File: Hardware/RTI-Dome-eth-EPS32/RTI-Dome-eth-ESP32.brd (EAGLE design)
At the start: 111.1 x 76.3 mm, 100 parts, among them IC1 REG1117FA-5.0_500, IC2 24LC64T-I/SN, IC8 REG1117-3.3V, J2 XT60PW-M, T1 MMBT3904LT1, T2 MMBT3904LT1, T3 MMBT3904LT1, U1 W5500, U2 ESP32-DevKitC ESP32-WROOM-32U, X9 J1011F01PNL

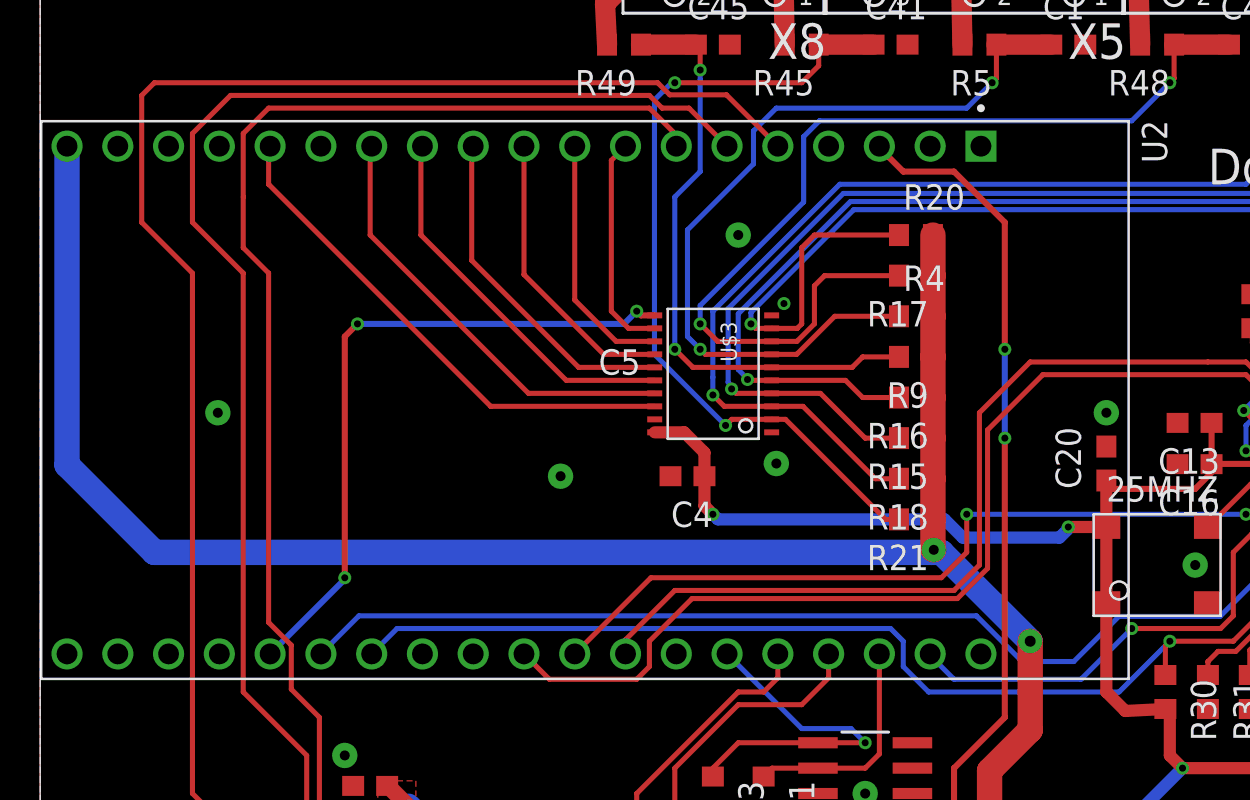
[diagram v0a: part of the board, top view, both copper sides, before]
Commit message: Set the proper version of the EXP32 kit for each board.
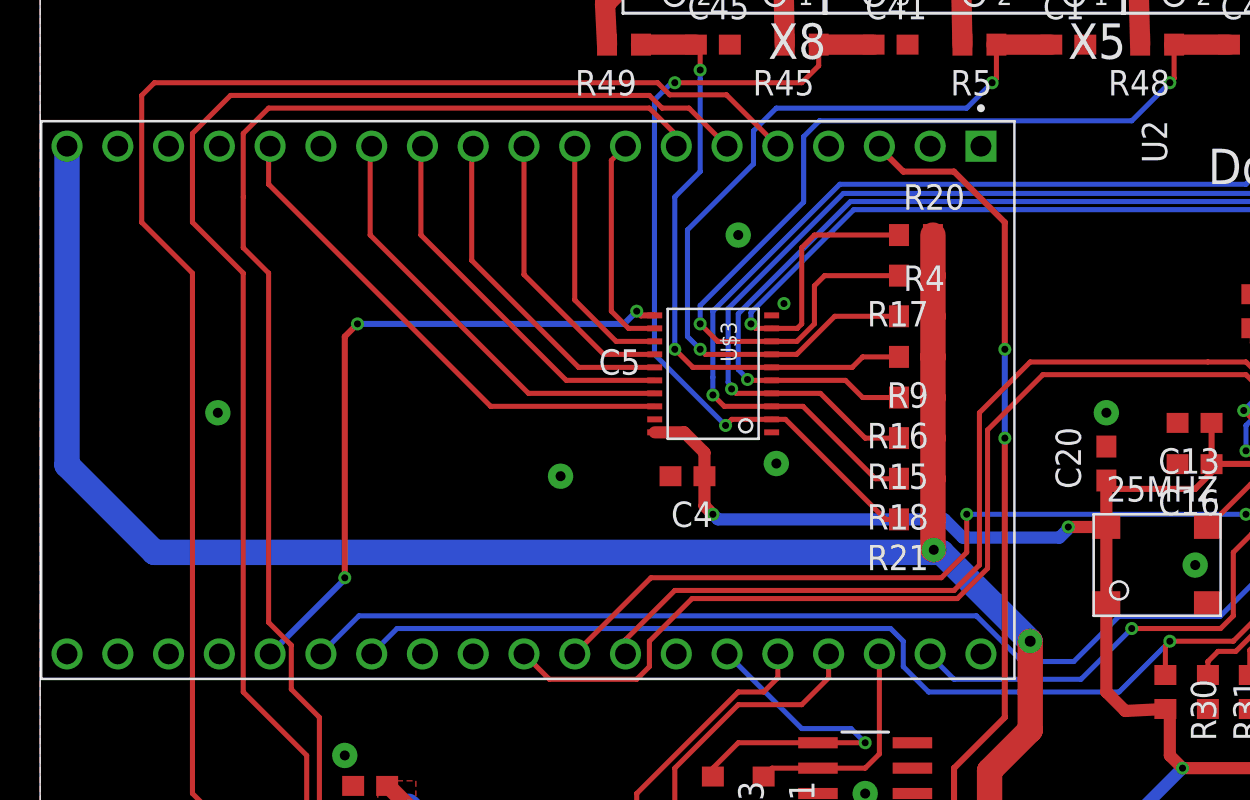
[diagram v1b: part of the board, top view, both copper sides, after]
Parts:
- U2: device ESP32-DEVKITC-32D:MODULE_ESP32-DEVKITC-32D -> ESP32-DEVKITC-32D:MODULE_ESP32-DEVKITC-32U
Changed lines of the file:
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@@
 <attribute name="VALUE" x="81.28" y="17" size="1.27" layer="27" align="center"/>
 </element>
-<element name="U2" library="ESP32-DEVKITC-32D" library_urn="urn:adsk.eagle:library:44270575" package="MODULE_ESP32-DEVKITC-32D" package3d_urn="urn:adsk.eagle:package:44270578/3" value="ESP32-DevKitC ESP32-WROOM-32U" x="27.305" y="46.99" smashed="yes" rot="R270">
-<attribute name="AVAILABILITY" value="In Stock" x="27.305" y="46.99" size="1.778" layer="27" rot="R270" display="off"/>
-<attribute name="CHECK_PRICES" value="https://www.snapeda.com/parts/ESP32-DEVKITC-32D/Espressif+Systems/view-part/?ref=eda" x="27.305" y="46.99" size="1.778" layer="27" rot="R270" display="off"/>
-<attribute name="DESCRIPTION" value=" WiFi Development Tools (802.11) ESP32 General Development Kit, ESP32-WROOM-32D on the board " x="27.305" y="46.99" size="1.778" layer="27" rot="R270" display="off"/>
-<attribute name="MF" value="Espressif Systems" x="27.305" y="46.99" size="1.778" layer="27" rot="R270" display="off"/>
-<attribute name="MP" value="ESP32-DEVKITC-32D" x="27.305" y="46.99" size="1.778" layer="27" rot="R270" display="off"/>
+<element name="U2" library="ESP32-DEVKITC-32D" library_urn="urn:adsk.eagle:library:44270575" package="MODULE_ESP32-DEVKITC-32U" package3d_urn="urn:adsk.eagle:package:44294361/2" value="ESP32-DevKitC ESP32-WROOM-32U" x="27.305" y="46.99" smashed="yes" rot="R270">
 <attribute name="NAME" x="55.1158" y="60.9954" size="1.270490625" layer="25" rot="R270"/>
-<attribute name="PACKAGE" value="None" x="27.305" y="46.99" size="1.778" layer="27" rot="R270" display="off"/>
-<attribute name="PRICE" value="None" x="27.305" y="46.99" size="1.778" layer="27" rot="R270" display="off"/>
-<attribute name="SNAPEDA_LINK" value="https://www.snapeda.com/parts/ESP32-DEVKITC-32D/Espressif+Systems/view-part/?ref=snap" x="27.305" y="46.99" size="1.778" layer="27" rot="R270" display="off"/>
 <attribute name="VALUE" x="-1.6252" y="61.0046" size="1.27133125" layer="27" rot="R270"/>
 </element>

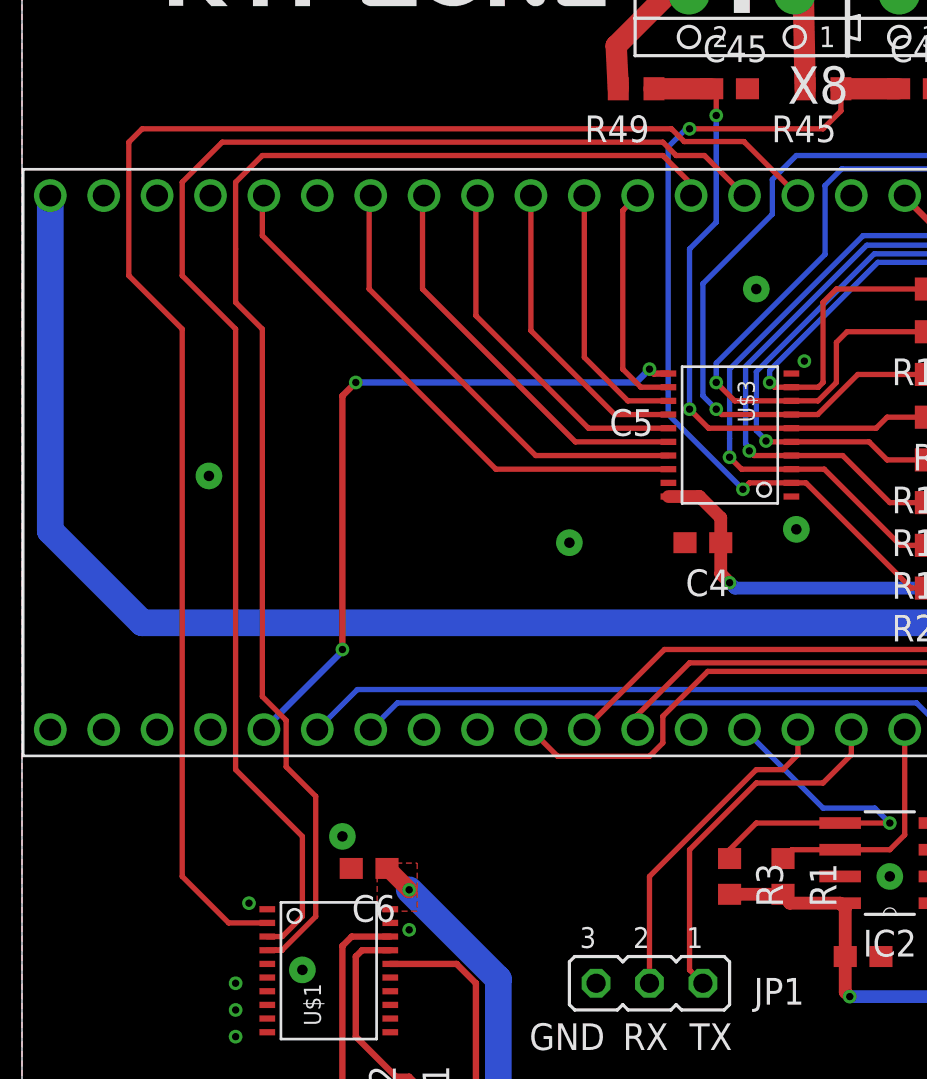
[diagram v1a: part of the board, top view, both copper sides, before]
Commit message: Fix pin assignement issues for ESP32
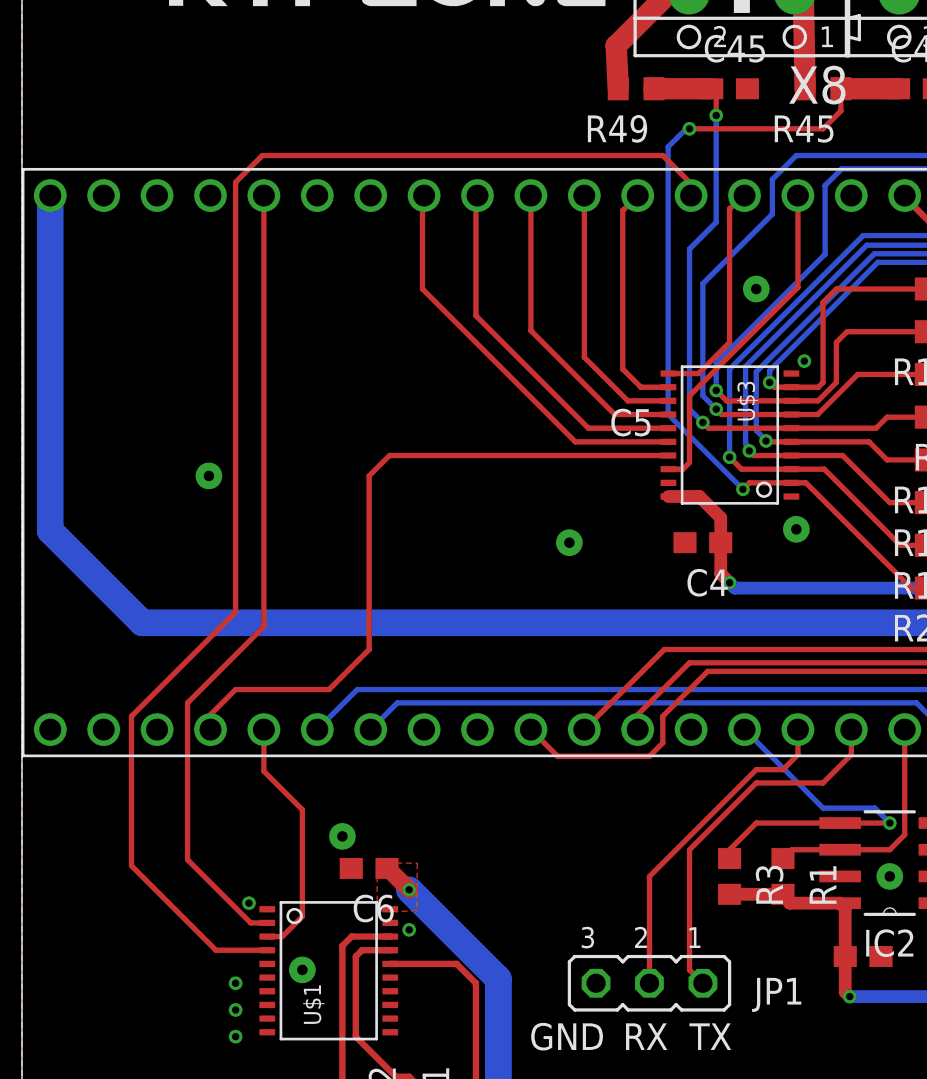
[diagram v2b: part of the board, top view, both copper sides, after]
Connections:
- removed net N$15: U2.23
- net AT_PARK_PIN: now also U2.6; no longer U2.24
- net HOME_SHUTTER_CLOSED: now also U2.23; no longer U2.13
- net M_DIR: now also U2.24; no longer U2.6
- net M_EN: now also U2.15; no longer U2.5
- net SPARE1: now also U2.5; no longer U2.15
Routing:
- net M_DIR: track 67.9 -> 11.7 mm
- net M_EN: track 74.3 -> 38.1 mm
- net AT_PARK_PIN: track 33.5 -> 10.8 mm, vias 3 -> 0
- net HOME_SHUTTER_CLOSED: track 22.0 -> 32.4 mm
- net SPARE1: track 25.9 -> 16.0 mm
- net M_STEP: track 63.1 -> 66.0 mm

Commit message: Fixed a lot of issue with the ESP32 and serial ports.
Alpaca Discovery and API server are now running in their own tasks.
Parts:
- added X7: (no value), rti:AK500/3
- moved R7 4.02 mm to (71.1, 6.99)
- moved R8 4.02 mm to (73.7, 6.99)
- moved R2 2.84 mm to (71.1, 10.2)
- moved R10 2.84 mm to (73.7, 10.2)
- moved R6 2.84 mm to (68.6, 10.2)
- moved R22 1.42 mm to (17.8, 15.2)
- moved R3 0.38 mm to (34.0, 27.3)
- moved C6 0.25 mm to (16.8, 27.7)
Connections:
- new net SPARE_OUT1: U$1.P$5, U2.25
- new net SPARE_OUT1_5V: U$1.P$15, X7.3
- new net SPARE_OUT2: U$1.P$6, U2.13
- new net SPARE_OUT2_5V: U$1.P$14, X7.2
- net GND: now also X7.1; no longer U$1.P$5, U$1.P$6
- net INT_N: no longer U2.25
- net RX2: now also JP1.2
- net RXD0: no longer JP1.2
- net TX2: now also JP1.1
- net TXD0: no longer JP1.1
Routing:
- net SPARE_OUT1_5V: track 0.00 -> 64.8 mm, vias 0 -> 2
- net SPARE_OUT2_5V: track 0.00 -> 58.4 mm, vias 0 -> 2
- net INT_N: track 52.7 -> 0.00 mm, vias 1 -> 0
- net SPARE_OUT2: track 0.00 -> 40.5 mm, vias 0 -> 2
- net TX2: track 0.00 -> 19.1 mm
- net RX2: track 0.00 -> 19.1 mm
- net TXD0: track 17.4 -> 0.00 mm
- net RXD0: track 15.7 -> 0.00 mm
- net SPARE_OUT1: track 0.00 -> 12.9 mm
- net N$5: track 2.74 -> 1.48 mm
- net N$3: track 2.74 -> 1.48 mm
- net +12V: track 165.2 -> 166.0 mm
- net VPIN: track 78.0 -> 77.4 mm

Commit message: Latest board fixes with the extra output for lower shutter/other things.
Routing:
- net VCC: track 255.1 -> 255.9 mm
- net SPARE_OUT2: track 40.5 -> 39.8 mm
- net BUTTON_EAST_OPEN: track 17.1 -> 16.5 mm
- net BUTTON_WEST_CLOSE: track 19.2 -> 18.5 mm
- net SPARE2: track 14.6 -> 14.0 mm
- net SDI: track 54.7 -> 54.1 mm
- net SPARE2_IN_5V: track 30.4 -> 30.9 mm
- net ETH_CS: track 57.7 -> 57.2 mm
